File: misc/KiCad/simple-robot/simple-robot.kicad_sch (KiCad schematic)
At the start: 69 parts, among them J1 MotLA, J10 Screw_Terminal_2_P5.00mm, J11 JSTHCSR04, J12 IR_RF, J13 IR_LF, J14 JST_GV, J15 JST RF_Logic, J16 JST RF_PWR, J2 MotLB, J3 JST03 Servo, J4 MotRA, J5 MotRB, J6 ENC_LF, J7 ENC_LR, J8 ENC_RF, J9 ENC_RR, P1 Port Expander, SW1 RotaryEncoder_Switch, U1 Pico2, U2 CD4049UB

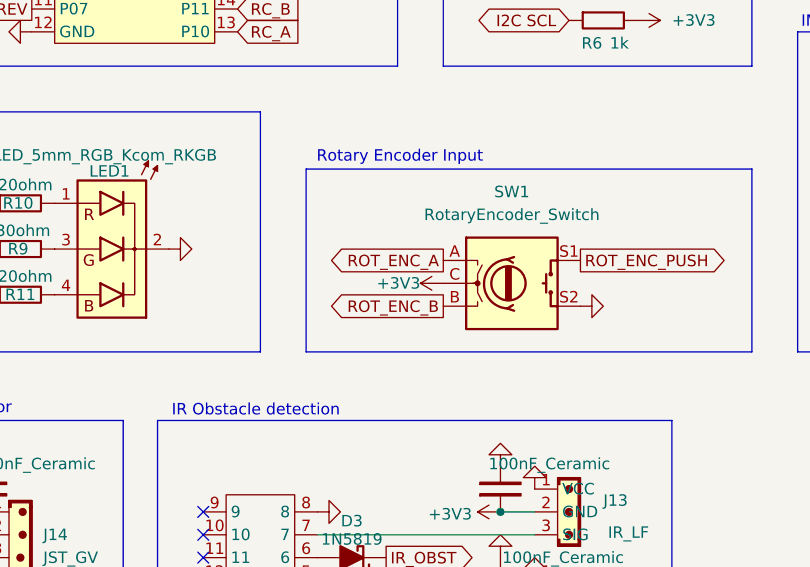
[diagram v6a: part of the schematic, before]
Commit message: rp235x E9 erratum hitting: rotary encoder should be reffed to common GND instead of 3V3
Pulldowns on RP235x only work on after stepping A4, all my boards are
stepping A2. So thereference for the encoder should not be 3V3 because
that we will need to pull down and that will latch on the RP.

Workaround is to add pulldowns which i will do for now but a proper
workaround is to change the pcb and schematic to have a common GND
instead of common 3V3 on the encoder and use pullup.

This commit changes schematic and pcb.
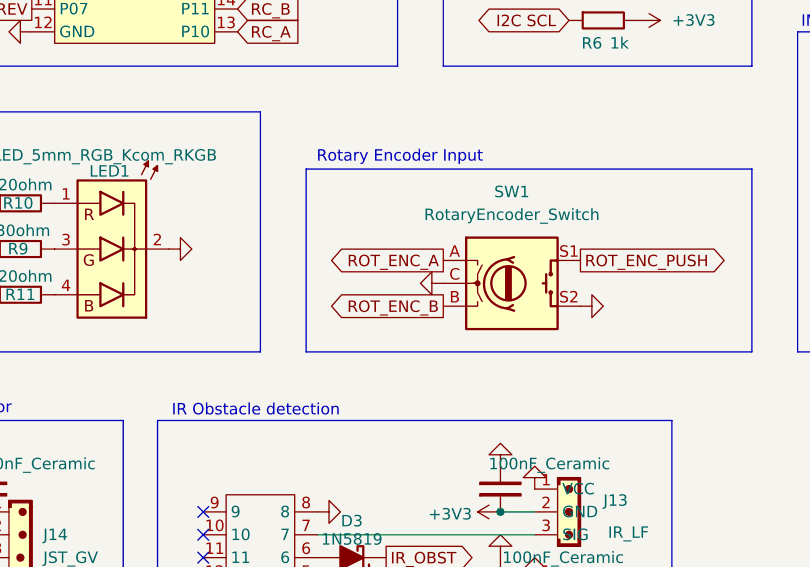
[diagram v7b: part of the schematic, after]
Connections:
- net +3V3: no longer SW1.C
- net GND: now also SW1.C
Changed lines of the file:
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@@
 	(title_block
 		(title "simple-robot")
-		(date "2026-01-26")
-		(rev "4")
+		(date "2026-02-22")
+		(rev "5")
 		(company "Rafael Koch")
 	)
@@
 	)
 	(symbol
-		(lib_id "power:+3V3")
-		(at 147.32 135.89 90)
-		(unit 1)
-		(exclude_from_sim no)
-		(in_bom yes)
-		(on_board yes)
-		(dnp no)
-		(fields_autoplaced yes)
-		(property "Reference" "#PWR011"
-			(at 151.13 135.89 0)
-			(effects
-				(font
-					(size 1.27 1.27)
-				)
-				(hide yes)
-			)
-		)
-		(property "Value" "+3V3"
-			(at 144.78 135.8899 90)
-			(effects
-				(font
-					(size 1.27 1.27)
-				)
-				(justify left)
-			)
-		)
-		(property "Footprint" ""
-			(at 147.32 135.89 0)
-			(effects
-				(font
-					(size 1.27 1.27)
-				)
-				(hide yes)
-			)
-		)
-		(property "Datasheet" ""
-			(at 147.32 135.89 0)
-			(effects
-				(font
-					(size 1.27 1.27)
-				)
-				(hide yes)
-			)
-		)
-		(property "Description" "Power symbol creates a global label with name \"+3V3\""
-			(at 147.32 135.89 0)
-			(effects
-				(font
-					(size 1.27 1.27)
-				)
-				(hide yes)
-			)
-		)
-		(pin "1"
-		)
-		(instances
-			(project "simple-robot"
-				(path "/bab01379-5d77-437e-95b1-5e737eb23384"
-					(reference "#PWR011")
-					(unit 1)
-				)
-			)
-		)
-	)
-	(symbol
 		(lib_id "Mechanical:MountingHole_Pad")
 		(at 158.75 33.02 0)
@@
 					(unit 1)
 				)
+			)
+		)
+	)
+	(symbol
+		(lib_id "power:GND")
+		(at 147.32 135.89 270)
+		(unit 1)
+		(exclude_from_sim no)
+		(in_bom yes)
+		(on_board yes)
+		(dnp no)
+		(property "Reference" "#PWR011"
+			(at 140.97 135.89 0)
+			(effects
+				(font
+					(size 1.27 1.27)
+				)
+				(hide yes)
+			)
+		)
+		(property "Value" "GND"
+			(at 143.51 136.652 0)
+			(effects
+				(font
+					(size 1.27 1.27)
+				)
+				(justify right)
+				(hide yes)
+			)
+		)
+		(property "Footprint" ""
+			(at 147.32 135.89 0)
+			(effects
+				(font
+					(size 1.27 1.27)
+				)
+				(hide yes)
+			)
+		)
+		(property "Datasheet" ""
+			(at 147.32 135.89 0)
+			(effects
+				(font
+					(size 1.27 1.27)
+				)
+				(hide yes)
+			)
+		)
+		(property "Description" "Power symbol creates a global label with name \"GND\" , ground"
+			(at 147.32 135.89 0)
+			(effects
+				(font
+					(size 1.27 1.27)
+				)
+				(hide yes)
+			)
+		)
+		(pin "1"
+		)
+		(instances
+			(project "simple-robot"
+				(path "/bab01379-5d77-437e-95b1-5e737eb23384"
+					(reference "#PWR011")
+					(unit 1)
+				)

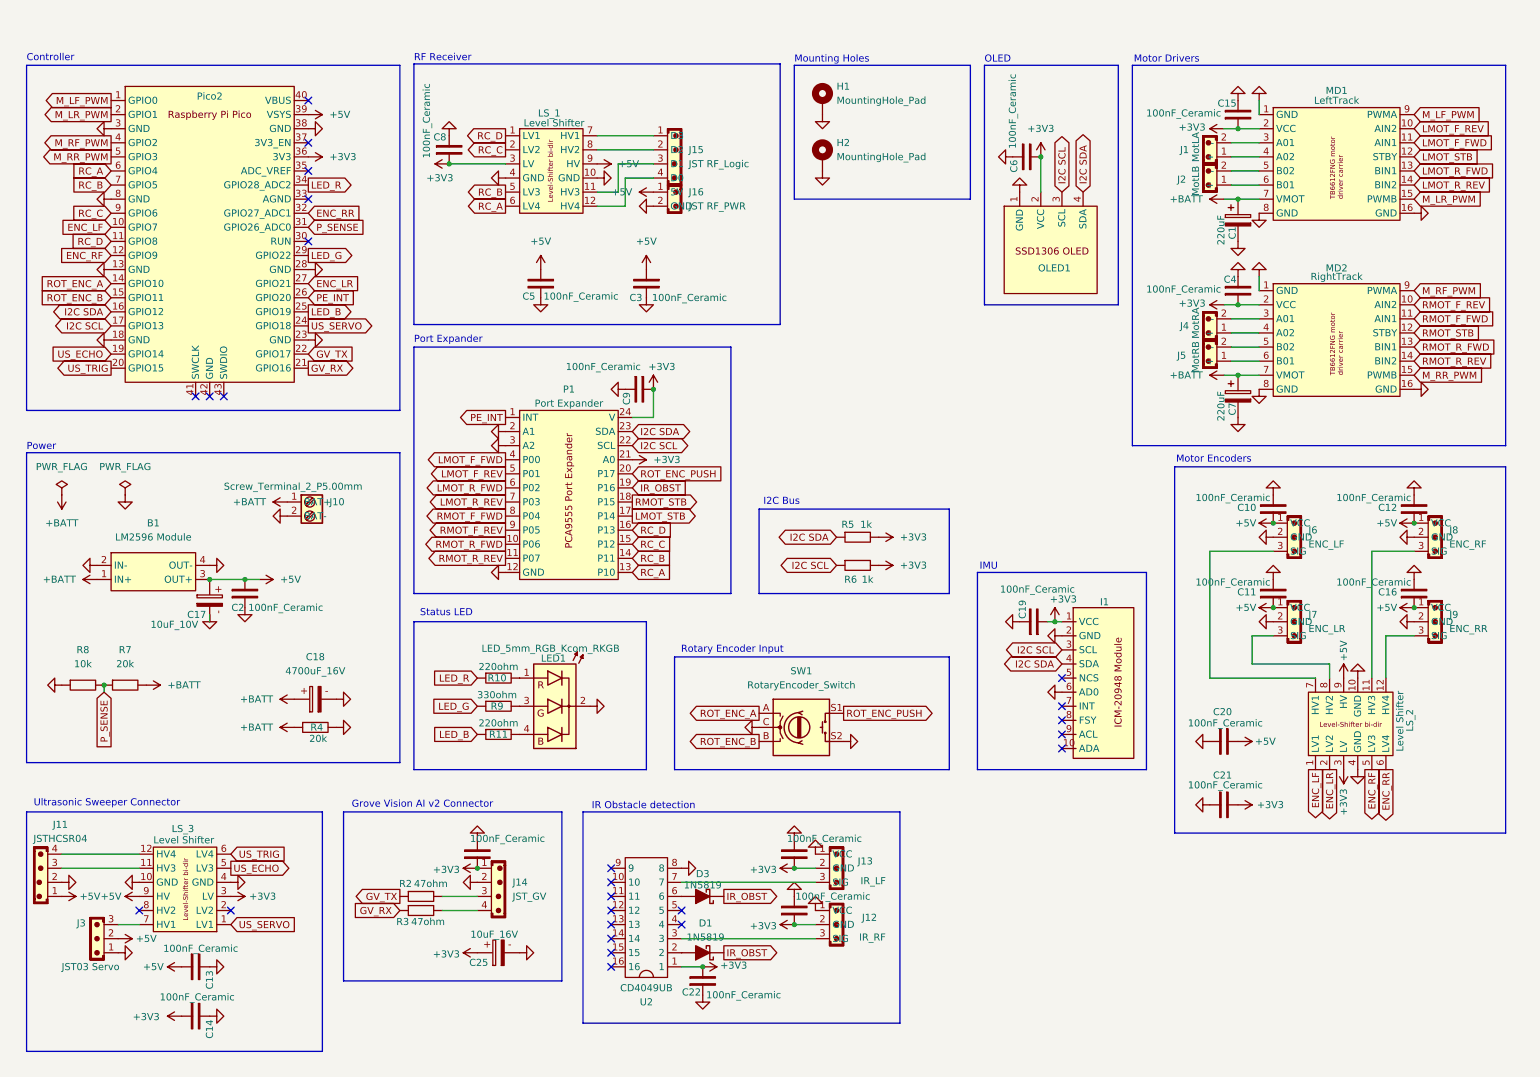
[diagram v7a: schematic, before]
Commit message: Ir us testmode (#33)
* new testmode for ultrasonic and ir sensors

* misassigned trig and echo pins fixed

* obstacle detection should blink the indicator

* Update schematic and pcb: IR_OBST net needs to be pulled low

* add ultrasonic sweep test mode

* The US measurements must not assume maximum distance if timing or
erroring out, in that case we simply have no data which represents cases
better, where we measure >maxdistance

* break test mode into more files, no blanket spawning of all test modes

* do not use us measurement >200cm

* dislay ownership conflict

* guard against running two testmode tasks simultaneously

* do not leak us values into later uses

* indicate obstacve and no obstacle

* clearer naming for test modes

* sweep was ONE line too long

* fmt

* review
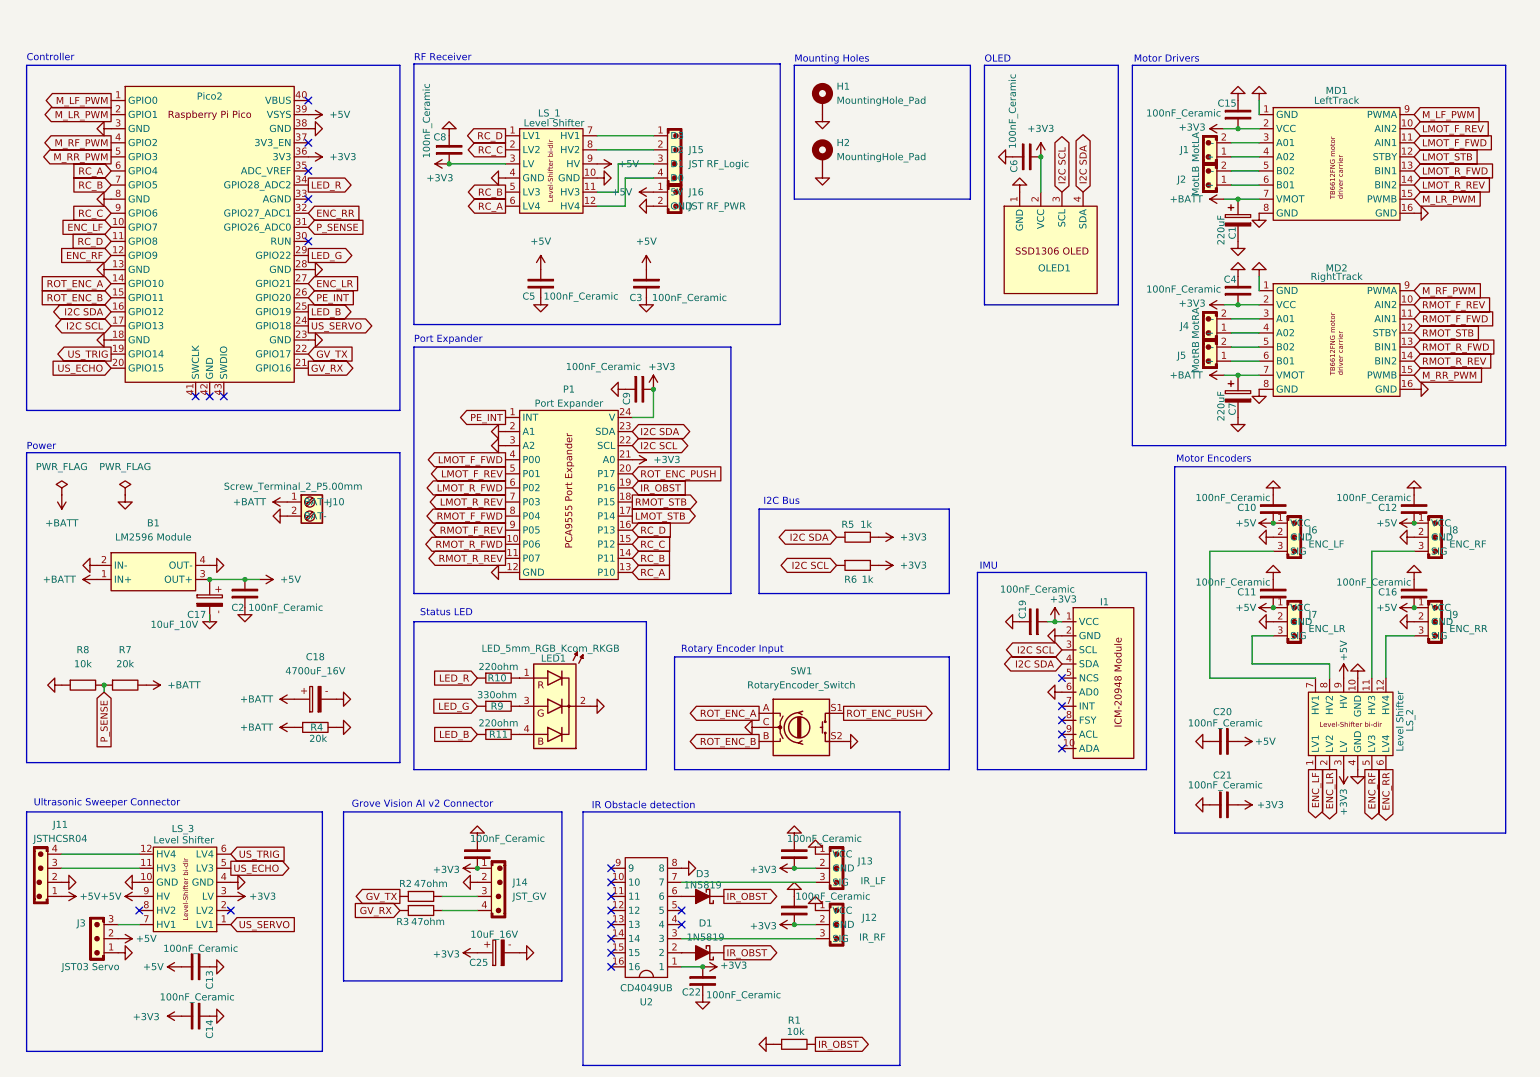
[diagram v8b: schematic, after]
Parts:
- added R1: 10k, Resistor_THT:R_Axial_DIN0207_L6.3mm_D2.5mm_P10.16mm_Horizontal, symbol PCM_SL_Resistors:10k
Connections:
- net GND: now also R1.1
- net IR_OBST: now also R1.2
- net US_ECHO: now also U1.20 (GPIO15); no longer U1.19 (GPIO14)
- net US_TRIG: now also U1.19 (GPIO14); no longer U1.20 (GPIO15)
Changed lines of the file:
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@@
 	(title_block
 		(title "simple-robot")
-		(date "2026-02-22")
-		(rev "5")
+		(date "2026-03-03")
+		(rev "6")
 		(company "Rafael Koch")
 	)
@@
 	(rectangle
 		(start 115.57 151.13)
-		(end 172.72 189.23)
+		(end 172.72 196.85)
 		(stroke
 			(width 0)
@@
 		)
 	)
-	(global_label "US_TRIG"
-		(shape output)
-		(at 30.48 71.12 180)
+	(global_label "RC_B"
+		(shape input)
+		(at 124.46 105.41 0)
 		(fields_autoplaced yes)
 		(effects
@@
 				(size 1.27 1.27)
 			)
-			(justify right)
+			(justify left)
 		)
 		(property "Intersheetrefs" "${INTERSHEET_REFS}"
-			(at 19.8748 71.12 0)
+			(at 132.2228 105.41 0)
 			(effects
 				(font
 					(size 1.27 1.27)
 				)
-				(justify right)
+				(justify left)
 				(hide yes)
 			)
 		)
 	)
-	(global_label "RC_B"
-		(shape input)
-		(at 124.46 105.41 0)
+	(global_label "IR_OBST"
+		(shape output)
+		(at 157.48 193.04 0)
 		(fields_autoplaced yes)
 		(effects
@@
 		)
 		(property "Intersheetrefs" "${INTERSHEET_REFS}"
-			(at 132.2228 105.41 0)
+			(at 168.0852 193.04 0)
 			(effects
 				(font
@@
 		)
 	)
-	(global_label "US_ECHO"
-		(shape input)
-		(at 30.48 68.58 180)
-		(fields_autoplaced yes)
-		(effects
-			(font
-				(size 1.27 1.27)
-			)
-			(justify right)
-		)
-		(property "Intersheetrefs" "${INTERSHEET_REFS}"
-			(at 18.9072 68.58 0)
-			(effects
-				(font
-					(size 1.27 1.27)
-				)
-				(justify right)
-				(hide yes)
-			)
-		)
-	)
 	(global_label "RC_C"
 		(shape input)
@@
 		)
 	)
+	(global_label "US_TRIG"
+		(shape output)
+		(at 30.48 68.58 180)
+		(fields_autoplaced yes)
+		(effects
+			(font
+				(size 1.27 1.27)
+			)
+			(justify right)
+		)
+		(property "Intersheetrefs" "${INTERSHEET_REFS}"
+			(at 19.8748 68.58 0)
+			(effects
+				(font
+					(size 1.27 1.27)
+				)
+				(justify right)
+				(hide yes)
+			)
+		)
+	)
 	(global_label "IR_OBST"
 		(shape output)
@@
 		)
 	)
+	(global_label "US_ECHO"
+		(shape input)
+		(at 30.48 71.12 180)
+		(fields_autoplaced yes)
+		(effects
+			(font
+				(size 1.27 1.27)
+			)
+			(justify right)
+		)
+		(property "Intersheetrefs" "${INTERSHEET_REFS}"
+			(at 18.9072 71.12 0)
+			(effects
+				(font
+					(size 1.27 1.27)
+				)
+				(justify right)
+				(hide yes)
+			)
+		)
+	)
 	(global_label "LMOT_STB"
 		(shape input)
@@
 	)
 	(symbol
+		(lib_id "PCM_SL_Resistors:10k")
+		(at 153.67 193.04 0)
+		(unit 1)
+		(exclude_from_sim no)
+		(in_bom yes)
+		(on_board yes)
+		(dnp no)
+		(property "Reference" "R1"
+			(at 153.67 188.722 0)
+			(effects
+				(font
+					(size 1.27 1.27)
+				)
+			)
+		)
+		(property "Value" "10k"
+			(at 153.924 190.754 0)
+			(effects
+				(font
+					(size 1.27 1.27)
+				)
+			)
+		)
+		(property "Footprint" "Resistor_THT:R_Axial_DIN0207_L6.3mm_D2.5mm_P10.16mm_Horizontal"
+			(at 154.559 197.358 0)
+			(effects
+				(font
+					(size 1.27 1.27)
+				)
+				(hide yes)
+			)
+		)
+		(property "Datasheet" ""
+			(at 154.178 193.04 0)
+			(effects
+				(font
+					(size 1.27 1.27)
+				)
+				(hide yes)
+			)
+		)
+		(property "Description" "10kΩ, 1/4W Resistor"
+			(at 153.67 193.04 0)
+			(effects
+				(font
+					(size 1.27 1.27)
+				)
+				(hide yes)
+			)
+		)
+		(pin "2"
+		)
+		(pin "1"
+		)
+		(instances
+			(project "simple-robot"
+				(path "/bab01379-5d77-437e-95b1-5e737eb23384"
+					(reference "R1")
+					(unit 1)
+				)
+			)
+		)
+	)
+	(symbol
 		(lib_id "power:+BATT")
 		(at 231.14 72.39 90)
@@
 					(unit 1)
 				)
+			)
+		)
+	)
+	(symbol
+		(lib_id "power:GND")
+		(at 149.86 193.04 270)
+		(unit 1)
+		(exclude_from_sim no)
+		(in_bom yes)
+		(on_board yes)
+		(dnp no)
+		(property "Reference" "#PWR0117"
+			(at 143.51 193.04 0)
+			(effects
+				(font
+					(size 1.27 1.27)
+				)
+				(hide yes)
+			)
+		)
+		(property "Value" "GND"
+			(at 146.05 193.802 0)
+			(effects
+				(font
+					(size 1.27 1.27)
+				)
+				(justify right)
+				(hide yes)
+			)
+		)
+		(property "Footprint" ""
+			(at 149.86 193.04 0)
+			(effects
+				(font
+					(size 1.27 1.27)
+				)
+				(hide yes)
+			)
+		)
+		(property "Datasheet" ""
+			(at 149.86 193.04 0)
+			(effects
+				(font
+					(size 1.27 1.27)
+				)
+				(hide yes)
+			)
+		)
+		(property "Description" "Power symbol creates a global label with name \"GND\" , ground"
+			(at 149.86 193.04 0)
+			(effects
+				(font
+					(size 1.27 1.27)
+				)
+				(hide yes)
+			)
+		)
+		(pin "1"
+		)
+		(instances
+			(project "simple-robot"
+				(path "/bab01379-5d77-437e-95b1-5e737eb23384"
+					(reference "#PWR0117")
+					(unit 1)
+				)
